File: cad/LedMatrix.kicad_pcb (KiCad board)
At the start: 2 copper layers, 76.2 x 63.5 mm, 74 parts, among them J1 Anodes, J2 GNDs

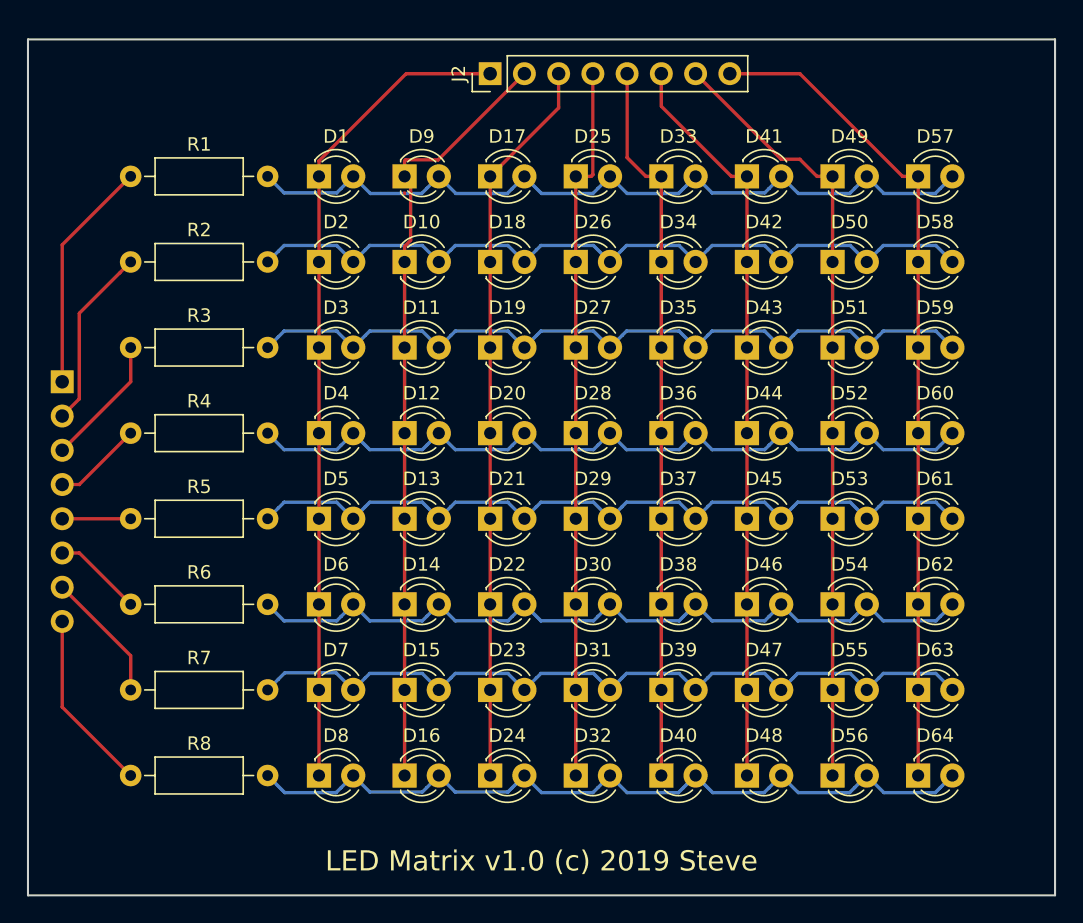
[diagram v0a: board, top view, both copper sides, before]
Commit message: add drill holes
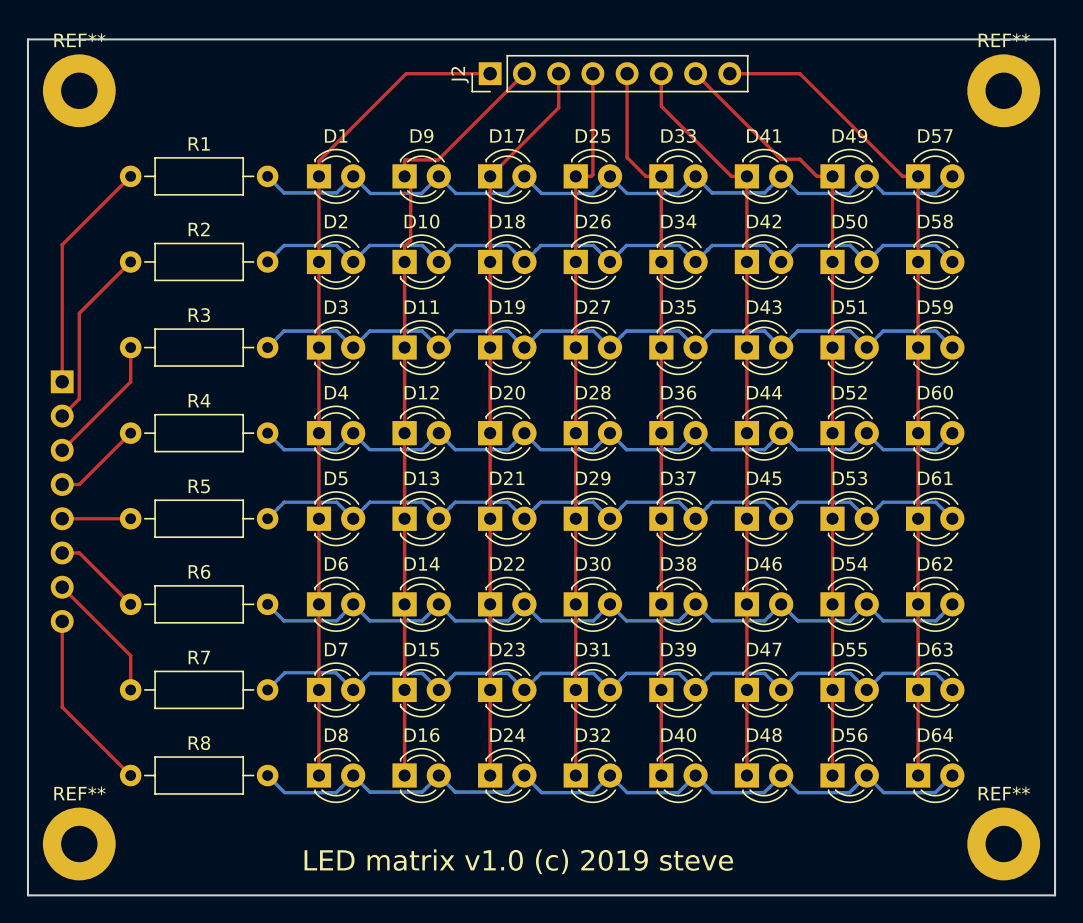
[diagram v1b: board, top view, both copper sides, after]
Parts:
- added REF**: MountingHole_2.7mm_M2.5_Pad, MountingHole:MountingHole_2.7mm_M2.5_Pad, F.Cu at (58.4, 29.2)
- added REF**: MountingHole_2.7mm_M2.5_Pad, MountingHole:MountingHole_2.7mm_M2.5_Pad, F.Cu at (58.4, 85.1)
- added REF**: MountingHole_2.7mm_M2.5_Pad, MountingHole:MountingHole_2.7mm_M2.5_Pad, F.Cu at (127.0, 85.1)
- added REF**: MountingHole_2.7mm_M2.5_Pad, MountingHole:MountingHole_2.7mm_M2.5_Pad, F.Cu at (127.0, 29.2)
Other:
- board text added: "LED matrix v1.0 (c) 2019 steve"
- board text removed: "LED Matrix v1.0 (c) 2019 Steve"
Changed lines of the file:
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@@
     (tracks 320)
     (zones 0)
-    (modules 74)
+    (modules 78)
     (nets 25)
   )
@@
     )
   )
+  (module MountingHole:MountingHole_2.7mm_M2.5_Pad (layer F.Cu)
+    (at 58.42 29.21)
+    (descr "Mounting Hole 2.7mm, M2.5")
+    (tags "mounting hole 2.7mm m2.5")
+    (attr virtual)
+    (fp_text reference REF** (at 0 -3.7) (layer F.SilkS)
+      (effects (font (size 1 1) (thickness 0.15)))
+    )
+    (fp_text value MountingHole_2.7mm_M2.5_Pad (at 0 3.7) (layer F.Fab) hide
+      (effects (font (size 1 1) (thickness 0.15)))
+    )
+    (fp_circle (center 0 0) (end 2.95 0) (layer F.CrtYd) (width 0.05))
+    (fp_circle (center 0 0) (end 2.7 0) (layer Cmts.User) (width 0.15))
+    (fp_text user %R (at 0.3 0) (layer F.Fab)
+      (effects (font (size 1 1) (thickness 0.15)))
+    )
+    (pad 1 thru_hole circle (at 0 0) (size 5.4 5.4) (drill 2.7) (layers *.Cu *.Mask))
+  )
+  (module MountingHole:MountingHole_2.7mm_M2.5_Pad (layer F.Cu)
+    (at 58.42 85.09)
+    (descr "Mounting Hole 2.7mm, M2.5")
+    (tags "mounting hole 2.7mm m2.5")
+    (attr virtual)
+    (fp_text reference REF** (at 0 -3.7) (layer F.SilkS)
+      (effects (font (size 1 1) (thickness 0.15)))
+    )
+    (fp_text value MountingHole_2.7mm_M2.5_Pad (at 0 3.7) (layer F.Fab) hide
+      (effects (font (size 1 1) (thickness 0.15)))
+    )
+    (fp_circle (center 0 0) (end 2.95 0) (layer F.CrtYd) (width 0.05))
+    (fp_circle (center 0 0) (end 2.7 0) (layer Cmts.User) (width 0.15))
+    (fp_text user %R (at 0.3 0) (layer F.Fab)
+      (effects (font (size 1 1) (thickness 0.15)))
+    )
+    (pad 1 thru_hole circle (at 0 0) (size 5.4 5.4) (drill 2.7) (layers *.Cu *.Mask))
+  )
+  (module MountingHole:MountingHole_2.7mm_M2.5_Pad (layer F.Cu)
+    (at 127 85.09)
+    (descr "Mounting Hole 2.7mm, M2.5")
+    (tags "mounting hole 2.7mm m2.5")
+    (attr virtual)
+    (fp_text reference REF** (at 0 -3.7) (layer F.SilkS)
+      (effects (font (size 1 1) (thickness 0.15)))
+    )
+    (fp_text value MountingHole_2.7mm_M2.5_Pad (at 0 3.7) (layer F.Fab) hide
+      (effects (font (size 1 1) (thickness 0.15)))
+    )
+    (fp_circle (center 0 0) (end 2.95 0) (layer F.CrtYd) (width 0.05))
+    (fp_circle (center 0 0) (end 2.7 0) (layer Cmts.User) (width 0.15))
+    (fp_text user %R (at 0.3 0) (layer F.Fab)
+      (effects (font (size 1 1) (thickness 0.15)))
+    )
+    (pad 1 thru_hole circle (at 0 0) (size 5.4 5.4) (drill 2.7) (layers *.Cu *.Mask))
+  )
+  (module MountingHole:MountingHole_2.7mm_M2.5_Pad (layer F.Cu)
+    (at 127 29.21)
+    (descr "Mounting Hole 2.7mm, M2.5")
+    (tags "mounting hole 2.7mm m2.5")
+    (attr virtual)
+    (fp_text reference REF** (at 0 -3.7) (layer F.SilkS)
+      (effects (font (size 1 1) (thickness 0.15)))
+    )
+    (fp_text value MountingHole_2.7mm_M2.5_Pad (at 0 3.7) (layer F.Fab) hide
+      (effects (font (size 1 1) (thickness 0.15)))
+    )
+    (fp_circle (center 0 0) (end 2.95 0) (layer F.CrtYd) (width 0.05))
+    (fp_circle (center 0 0) (end 2.7 0) (layer Cmts.User) (width 0.15))
+    (fp_text user %R (at 0.3 0) (layer F.Fab)
+      (effects (font (size 1 1) (thickness 0.15)))
+    )
+    (pad 1 thru_hole circle (at 0 0) (size 5.4 5.4) (drill 2.7) (layers *.Cu *.Mask))
+  )
+  (gr_text "LED matrix v1.0 (c) 2019 steve" (at 74.93 86.36) (layer F.SilkS)
+    (effects (font (size 1.5 1.5) (thickness 0.3)) (justify left))
+  )
   (dimension 63.5 (width 0.3) (layer F.Fab)
     (gr_text "63.500 mm" (at 144.34 57.15 270) (layer F.Fab)
@@
     (arrow2b (pts (xy 54.61 17.78) (xy 55.736504 17.193579)))
   )
-  (gr_text "LED Matrix v1.0 (c) 2019 Steve" (at 92.71 86.36) (layer F.SilkS)
-    (effects (font (size 1.5 1.5) (thickness 0.3)))
-  )
   (gr_line (start 54.61 88.9) (end 54.61 25.4) (layer Edge.Cuts) (width 0.15))
